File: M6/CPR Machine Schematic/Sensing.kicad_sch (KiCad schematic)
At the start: 0 parts

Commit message: ToF
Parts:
- added U7: VL53L0CXV0DH1, Sensor_Distance:ST_VL53L1x, symbol Sensor_Distance:VL53L0CXV0DH1
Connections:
- new net GND: U7.12 (GND), U7.3 (GND), U7.4 (GND), U7.6 (GND)
- new net I2C_SCL: U7.10 (SCL)
- new net I2C_SDA: U7.9 (SDA)
- no-connect marks 0 -> 4
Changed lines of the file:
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@@
 	(generator_version "9.0")
 	(paper "A4")
+	(no_connect
+		(at 87.63 63.5)
+	)
+	(no_connect
+		(at 64.77 50.8)
+	)
+	(no_connect
+		(at 95.25 50.8)
+	)
+	(no_connect
+		(at 64.77 53.34)
+	)
+	(hierarchical_label "I2C_SCL"
+		(shape input)
+		(at 82.55 63.5 270)
+		(effects
+			(font
+				(size 1.27 1.27)
+			)
+			(justify right)
+		)
+	)
+	(hierarchical_label "I2C_SDA"
+		(shape bidirectional)
+		(at 80.01 63.5 270)
+		(effects
+			(font
+				(size 1.27 1.27)
+			)
+			(justify right)
+		)
+	)
+	(symbol
+		(lib_id "Sensor_Distance:VL53L0CXV0DH1")
+		(at 80.01 53.34 90)
+		(unit 1)
+		(exclude_from_sim no)
+		(in_bom yes)
+		(on_board yes)
+		(dnp no)
+		(fields_autoplaced yes)
+		(property "Reference" "U7"
+			(at 80.01 40.64 90)
+			(effects
+				(font
+					(size 1.27 1.27)
+				)
+			)
+		)
+		(property "Value" "VL53L0CXV0DH1"
+			(at 80.01 43.18 90)
+			(effects
+				(font
+					(size 1.27 1.27)
+				)
+			)
+		)
+		(property "Footprint" "Sensor_Distance:ST_VL53L1x"
+			(at 93.98 36.195 0)
+			(effects
+				(font
+					(size 1.27 1.27)
+				)
+				(hide yes)
+			)
+		)
+		(property "Datasheet" "https://www.st.com/resource/en/datasheet/vl53l0x.pdf"
+			(at 80.01 50.8 0)
+			(effects
+				(font
+					(size 1.27 1.27)
+				)
+				(hide yes)
+			)
+		)
+		(property "Description" "2m distance ranging ToF sensor, Optical LGA12"
+			(at 80.01 53.34 0)
+			(effects
+				(font
+					(size 1.27 1.27)
+				)
+				(hide yes)
+			)
+		)
+		(pin "7"
+		)
+		(pin "8"
+		)
+		(pin "10"
+		)
+		(pin "9"
+		)
+		(pin "5"
+		)
+		(pin "4"
+		)
+		(pin "6"
+		)
+		(pin "1"
+		)
+		(pin "11"
+		)
+		(pin "12"
+		)
+		(pin "3"
+		)
+		(pin "2"
+		)
+		(instances
+			(project ""
+				(path "/8991fc77-975f-4978-a089-6b2a5e33f59b/2e704a40-db78-4cf7-9f7e-cfc586f5aeb3"
+					(reference "U7")
+					(unit 1)
+				)
+			)
+		)
+	)
+	(symbol
+		(lib_id "power:GND")
+		(at 95.25 53.34 0)
+		(unit 1)
+		(exclude_from_sim no)
+		(in_bom yes)
+		(on_board yes)
+		(dnp no)
+		(fields_autoplaced yes)
+		(property "Reference" "#PWR018"
+			(at 95.25 59.69 0)
+			(effects
+				(font
+					(size 1.27 1.27)
+				)
+				(hide yes)
+			)
+		)
+		(property "Value" "GND"
+			(at 95.25 58.42 0)
+			(effects
+				(font
+					(size 1.27 1.27)
+				)
+			)
+		)
+		(property "Footprint" ""
+			(at 95.25 53.34 0)
+			(effects
+				(font
+					(size 1.27 1.27)
+				)
+				(hide yes)
+			)
+		)
+		(property "Datasheet" ""
+			(at 95.25 53.34 0)
+			(effects
+				(font
+					(size 1.27 1.27)
+				)
+				(hide yes)
+			)
+		)
+		(property "Description" "Power symbol creates a global label with name \"GND\" , ground"
+			(at 95.25 53.34 0)
+			(effects
+				(font
+					(size 1.27 1.27)
+				)
+				(hide yes)
+			)
+		)
+		(pin "1"
+		)
+		(instances
+			(project ""
+				(path "/8991fc77-975f-4978-a089-6b2a5e33f59b/2e704a40-db78-4cf7-9f7e-cfc586f5aeb3"
+					(reference "#PWR018")
+					(unit 1)
+				)
+			)
+		)
+	)
 )

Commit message: More kiCAD
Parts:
- removed U7: VL53L0CXV0DH1, Sensor_Distance:ST_VL53L1x, symbol Sensor_Distance:VL53L0CXV0DH1
- added U7: Adafruit VL53L0X, symbol Custom_Parts:Adafruit_VL53L0X
- added U8: Adafruit IMU, 4754:MODULE_4754, symbol 4754:4754
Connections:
- net GND: now also U7. (XSHUT), U8.JP1_3 (GND)
- net I2C_SCL: now also U7. (XSHUT), U8.JP1_4 (SCL)
- net I2C_SDA: now also U7. (XSHUT), U8.JP1_5 (SDA)
- new net +5V: U7. (XSHUT), U8.JP1_1 (VIN)
- new net ToF_GPIO: U7. (XSHUT)
- no-connect marks 4 -> 9

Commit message: morer kicad
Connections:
- net ToF_GPIO is gone; now on net I2C_SDA: U7. (XSHUT)
- no-connect marks 9 -> 10
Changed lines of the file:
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@@
+	)
+	(no_connect
+		(at 86.36 57.15)
 	)
 	(no_connect
@@
 		(effects
 			(font
-				(size 1.27 1.27)
-			)
-			(justify right)
-		)
-	)
-	(hierarchical_label "ToF_GPIO"
-		(shape bidirectional)
-		(at 86.36 57.15 270)
-		(effects
-			(font

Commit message: HMI schem for real for real
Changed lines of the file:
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@@
+	(wire
+		(pts
+			(xy 118.11 64.77) (xy 81.28 64.77)
+		)
+		(stroke
+			(width 0)
+			(type default)
+		)
+	)
 	(wire
 		(pts
@@
 		)
 	)
+	(wire
+		(pts
+			(xy 81.28 64.77) (xy 81.28 57.15)
+		)
+		(stroke
+			(width 0)
+			(type default)
+		)
+	)
+	(wire
+		(pts
+			(xy 83.82 67.31) (xy 118.11 67.31)
+		)
+		(stroke
+			(width 0)
+			(type default)
+		)
+	)
+	(wire
+		(pts
+			(xy 83.82 57.15) (xy 83.82 67.31)
+		)
+		(stroke
+			(width 0)
+			(type default)
+		)
+	)
 	(hierarchical_label "I2C_SCL"
 		(shape input)
-		(at 83.82 57.15 270)
+		(at 99.06 64.77 90)
 		(effects
 			(font
 				(size 1.27 1.27)
 			)
-			(justify right)
-		)
-	)
-	(hierarchical_label "I2C_SCL"
-		(shape input)
-		(at 118.11 64.77 180)
-		(effects
-			(font
-				(size 1.27 1.27)
-			)
-			(justify right)
+			(justify left)
 		)
 	)
 	(hierarchical_label "I2C_SDA"
 		(shape bidirectional)
-		(at 81.28 57.15 270)
+		(at 99.06 67.31 270)
 		(effects
 			(font
-				(size 1.27 1.27)
-			)
-			(justify right)
-		)
-	)
-	(hierarchical_label "I2C_SDA"
-		(shape bidirectional)
-		(at 118.11 67.31 180)
-		(effects
-			(font

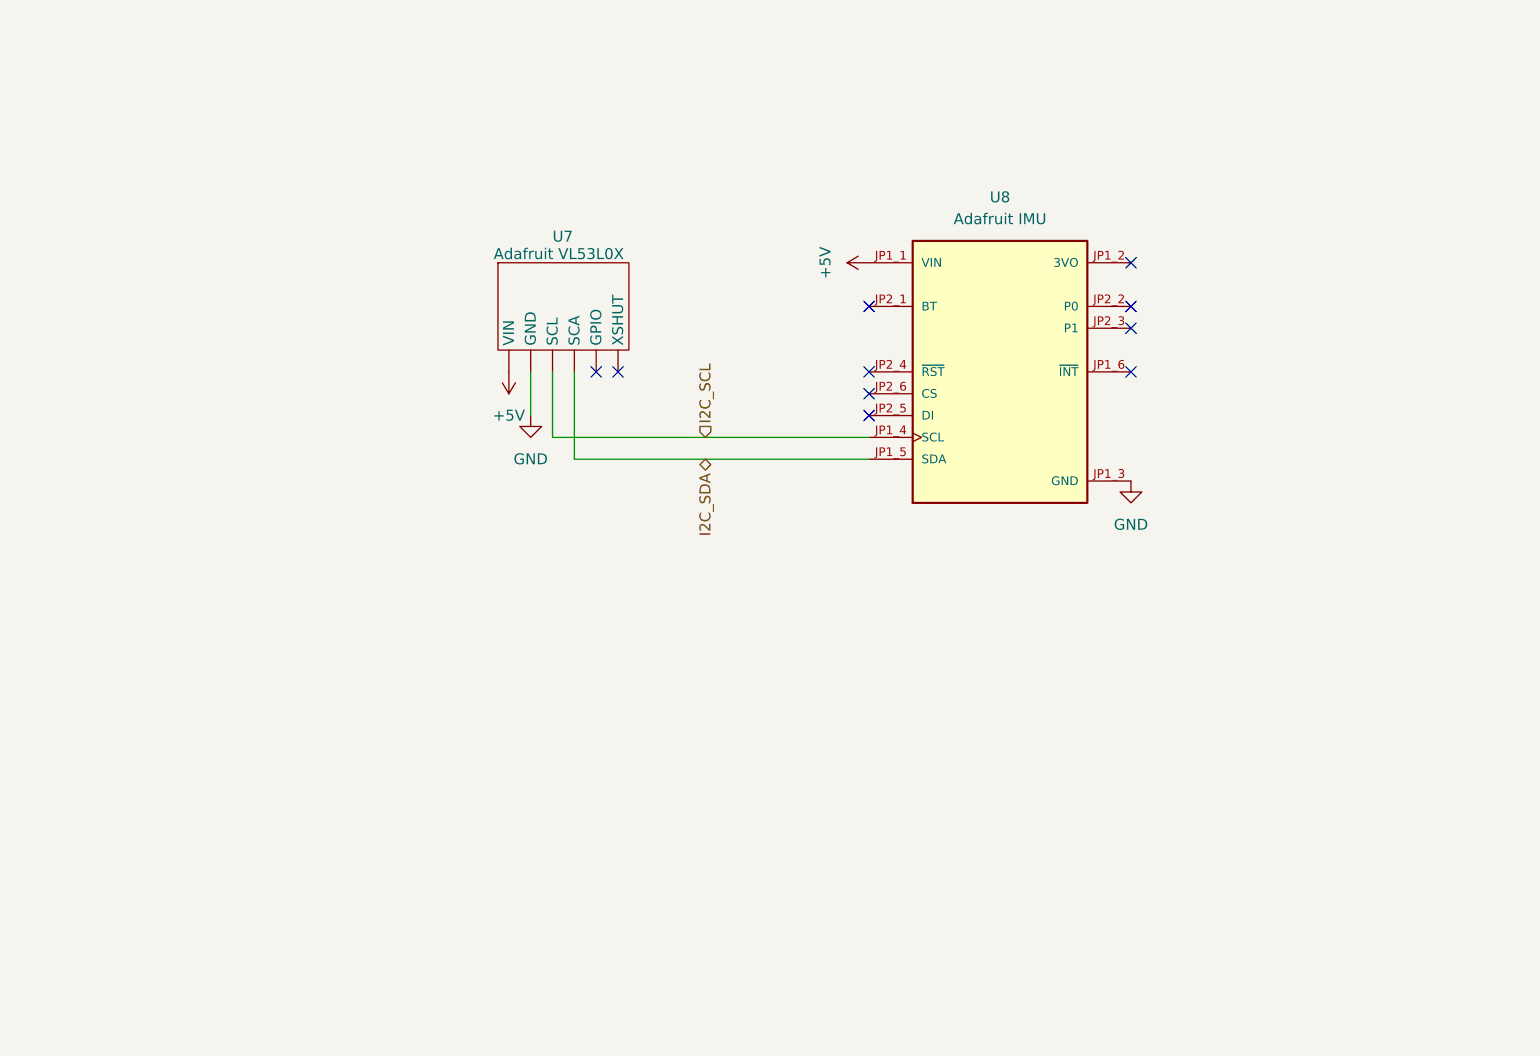
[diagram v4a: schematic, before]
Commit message: Single-pager KiCAD
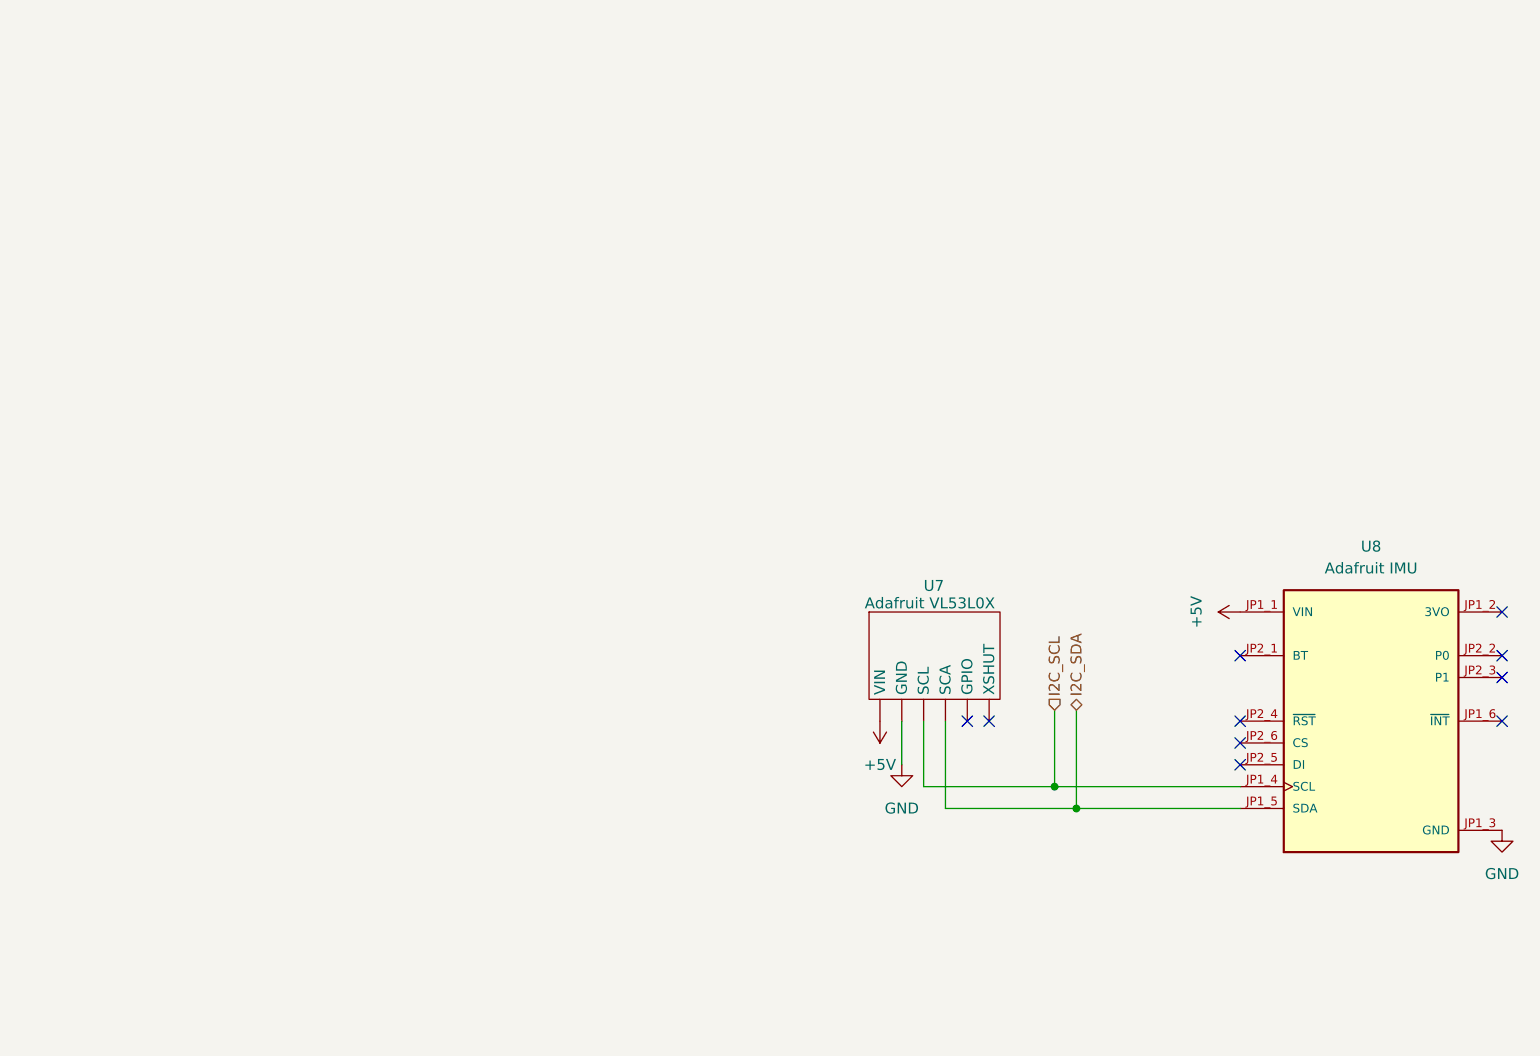
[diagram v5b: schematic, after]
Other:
- moved on the sheet: U7, U8

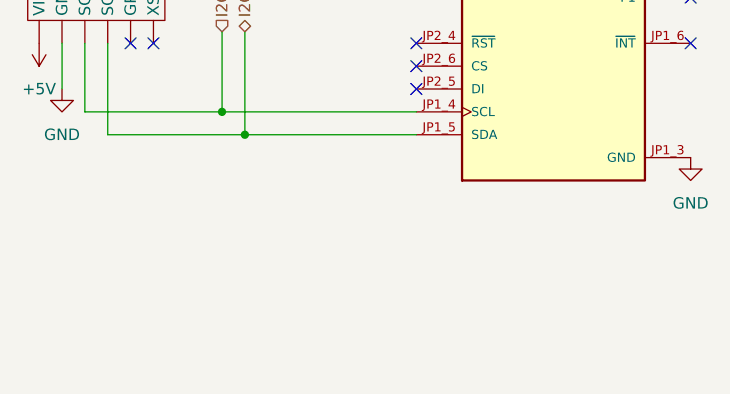
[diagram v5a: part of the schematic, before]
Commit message: force sensor oobs
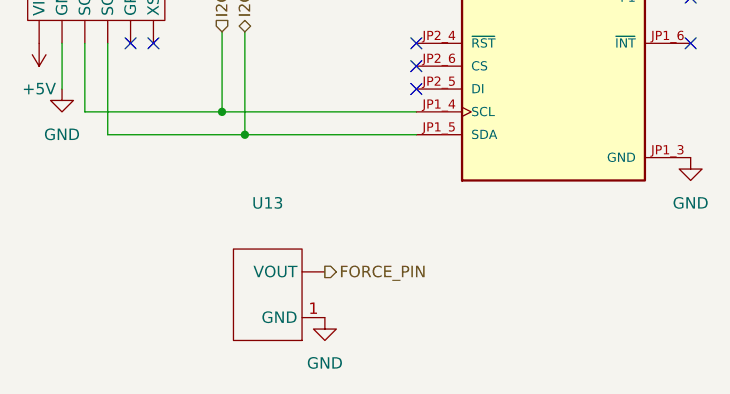
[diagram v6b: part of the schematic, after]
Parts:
- added U13: ~, symbol Custom_Parts:Force_Sensor
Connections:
- net GND: now also U13.1 (GND)
- new net FORCE_PIN: U13. (VOUT)
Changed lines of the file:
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@@
+		)
+	)
+	(hierarchical_label "FORCE_PIN"
+		(shape output)
+		(at 151.13 123.19 0)
+		(effects
+			(font
+				(size 1.27 1.27)
+			)
+			(justify left)
 		)
 	)
@@
 				(path "/8991fc77-975f-4978-a089-6b2a5e33f59b/2e704a40-db78-4cf7-9f7e-cfc586f5aeb3"
 					(reference "U7")
+					(unit 1)
+				)
+			)
+		)
+	)
+	(symbol
+		(lib_id "power:GND")
+		(at 151.13 128.27 0)
+		(unit 1)
+		(exclude_from_sim no)
+		(in_bom yes)
+		(on_board yes)
+		(dnp no)
+		(fields_autoplaced yes)
+		(property "Reference" "#PWR042"
+			(at 151.13 134.62 0)
+			(effects
+				(font
+					(size 1.27 1.27)
+				)
+				(hide yes)
+			)
+		)
+		(property "Value" "GND"
+			(at 151.13 133.35 0)
+			(effects
+				(font
+					(size 1.27 1.27)
+				)
+			)
+		)
+		(property "Footprint" ""
+			(at 151.13 128.27 0)
+			(effects
+				(font
+					(size 1.27 1.27)
+				)
+				(hide yes)
+			)
+		)
+		(property "Datasheet" ""
+			(at 151.13 128.27 0)
+			(effects
+				(font
+					(size 1.27 1.27)
+				)
+				(hide yes)
+			)
+		)
+		(property "Description" "Power symbol creates a global label with name \"GND\" , ground"
+			(at 151.13 128.27 0)
+			(effects
+				(font
+					(size 1.27 1.27)
+				)
+				(hide yes)
+			)
+		)
+		(pin "1"
+		)
+		(instances
+			(project ""
+				(path "/8991fc77-975f-4978-a089-6b2a5e33f59b/2e704a40-db78-4cf7-9f7e-cfc586f5aeb3"
+					(reference "#PWR042")
 					(unit 1)
 				)
@@
 					(unit 1)
 				)
+			)
+		)
+	)
+	(symbol
+		(lib_id "Custom_Parts:Force_Sensor")
+		(at 144.78 125.73 90)
+		(unit 1)
+		(exclude_from_sim no)
+		(in_bom yes)
+		(on_board yes)
+		(dnp no)
+		(fields_autoplaced yes)
+		(property "Reference" "U13"
+			(at 144.78 115.57 90)
+			(effects
+				(font
+					(size 1.27 1.27)
+				)
+			)
+		)
+		(property "Value" "~"
+			(at 144.78 118.11 90)
+			(effects
+				(font
+					(size 1.27 1.27)
+				)
+			)
+		)
+		(property "Footprint" ""
+			(at 144.78 125.73 0)
+			(effects
+				(font
+					(size 1.27 1.27)
+				)
+				(hide yes)
+			)
+		)
+		(property "Datasheet" ""
+			(at 144.78 125.73 0)
+			(effects
+				(font
+					(size 1.27 1.27)
+				)
+				(hide yes)
+			)
+		)
+		(property "Description" ""
+			(at 144.78 125.73 0)
+			(effects
+				(font
+					(size 1.27 1.27)
+				)
+				(hide yes)
+			)
+		)
+		(pin "1"
+		)
+		(pin ""
+		)
+		(instances
+			(project ""
+				(path "/8991fc77-975f-4978-a089-6b2a5e33f59b/2e704a40-db78-4cf7-9f7e-cfc586f5aeb3"
+					(reference "U13")
+					(unit 1)
+				)

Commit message: Start of Schematic V2
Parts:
- removed U13: ~, symbol Custom_Parts:Force_Sensor
- added J8: Conn_01x02_Pin, symbol Connector:Conn_01x02_Pin
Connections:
- net FORCE_PIN: now also J8.1 (Pin_1)
- net GND: now also J8.2 (Pin_2)
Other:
- note added: "Force Sensor & Op-Amps"
- note added: "I2C Sensors"
- moved on the sheet: U7, U8

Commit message: More PCB Progress
All Footprints
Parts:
- removed U7: Adafruit VL53L0X, symbol Custom_Parts:Adafruit_VL53L0X
- removed U8: Adafruit IMU, 4754:MODULE_4754, symbol 4754:4754
- added C13, C_OPT1: 47 pF, Capacitor_SMD:C_1206_3216Metric, symbol Device:C
- added J12: I2C Port, Connector_PinHeader_2.54mm:PinHeader_1x02_P2.54mm_Vertical, symbol Connector:Conn_01x02_Pin
- added R16: 10 kOhm, Resistor_SMD:R_1206_3216Metric, symbol Device:R_US
- added U3: MCP6001R, Package_TO_SOT_SMD:SOT-23-5, symbol Amplifier_Operational:MCP6001R
- J8: value Conn_01x02_Pin -> Force Sensor; footprint (none) -> TerminalBlock:TerminalBlock_MaiXu_MX126-5.0-02P_1x02_P5.00mm
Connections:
- net +5V: now also U3.2 (V+)
- net GND: now also C_OPT1.1, U3.3 (+), U3.5 (V-)
- net I2C_SCL: now also J12.2 (Pin_2)
- net I2C_SDA: now also J12.1 (Pin_1)
- net FORCE_PIN: no longer names the net of J8.1 (Pin_1)
- net FORCE_PIN: now also C13.1, R16.2, U3.4 (-)
- new net FORCE_IN: C13.2, C_OPT1.2, R16.1, U3.1
- no-connect marks 10 -> 0
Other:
- note added: "I2C Port"
- note removed: "I2C Sensors"
- moved on the sheet: J8
